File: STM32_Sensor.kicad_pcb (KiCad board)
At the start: 2 copper layers, 35.6 x 20.3 mm, 27 parts, among them J1 Conn Side, J2 Conn Down, J3 Conn Up, J4 Conn Prog, J5 u.FL, SW1 SW_Reset, SW2 SW_BOOT, U1 STM32F103C8Tx, U2 RFM69CW, U3 RFM69HW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

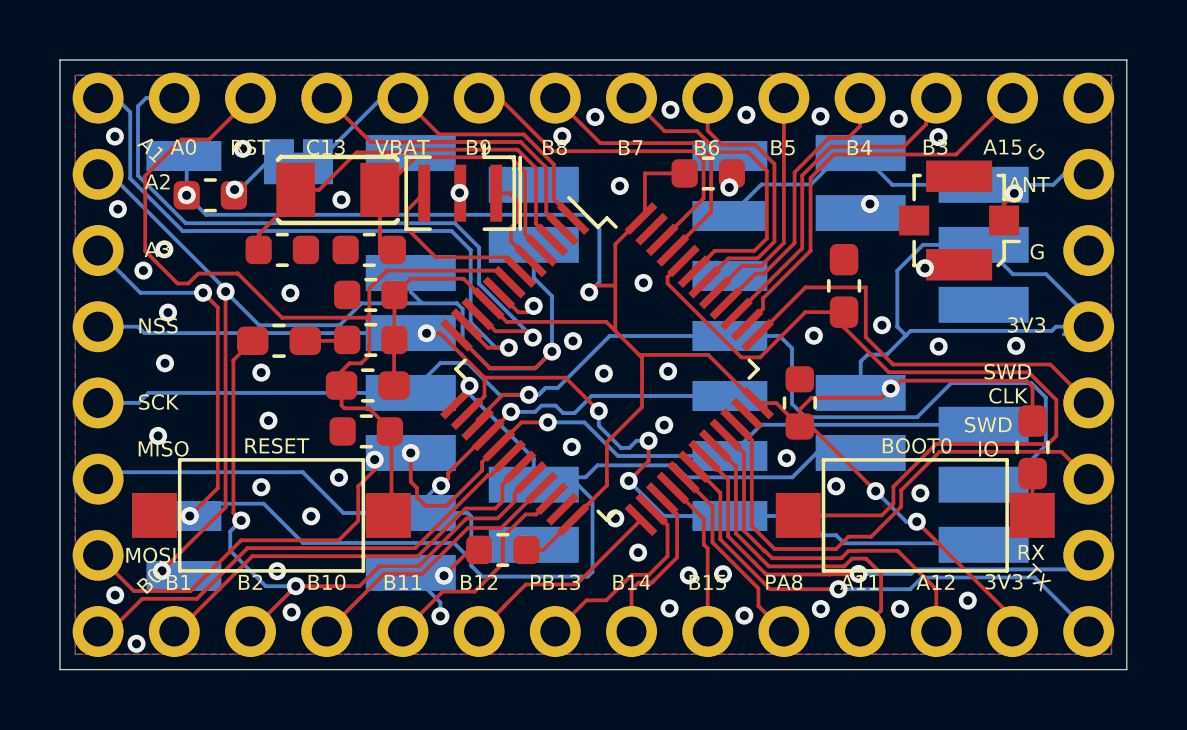
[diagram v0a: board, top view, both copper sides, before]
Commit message: Cleaned up project
Removed files that can be generated except for top and bottom
images which are referenced in the README.md
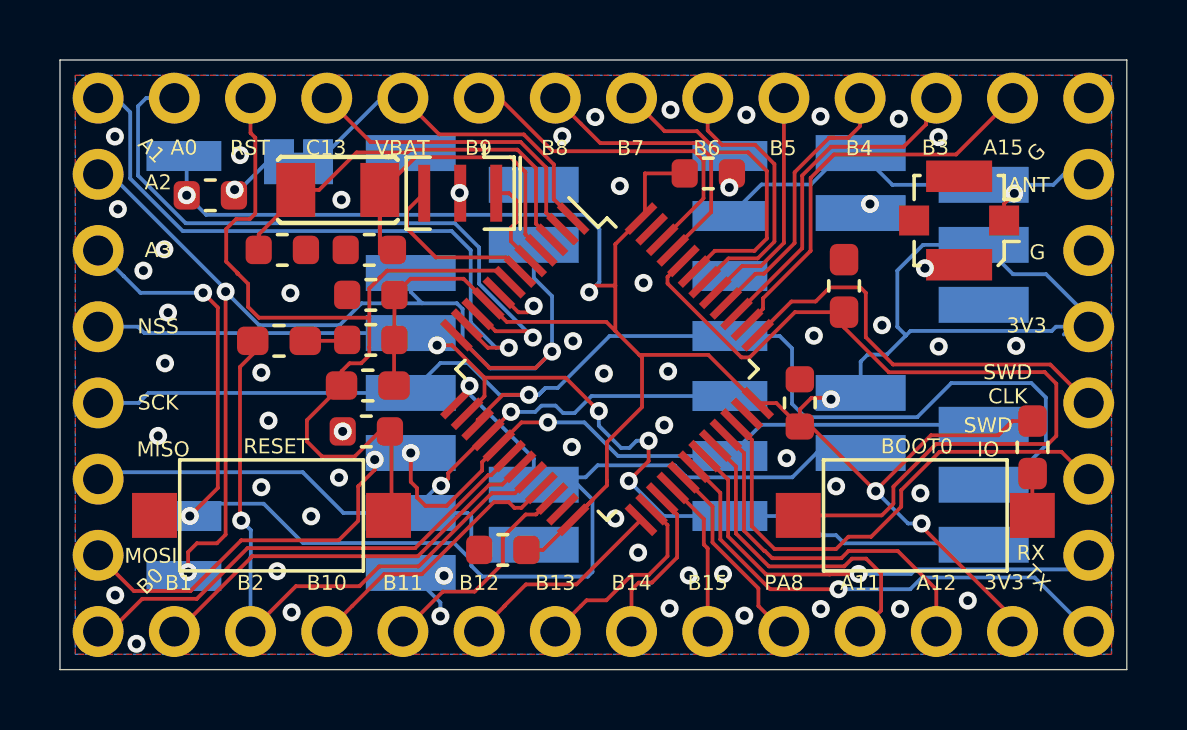
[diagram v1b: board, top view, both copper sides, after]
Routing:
- net +3V3: track 96.7 -> 94.8 mm
- net GND: track 7.47 -> 6.30 mm, vias 56 -> 57
- net RST: track 30.5 -> 29.9 mm
- net PB2: track 21.8 -> 21.5 mm, vias 2 -> 1
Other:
- board text added: "STM32 Sensor Node V5.0 by freynder"
- board text removed: "PB13"
- board text removed: "STM32 Sensor Node V4.5 by freynder"

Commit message: Made VBAT jumper NO
to comply with PCB manufacturer design rules.
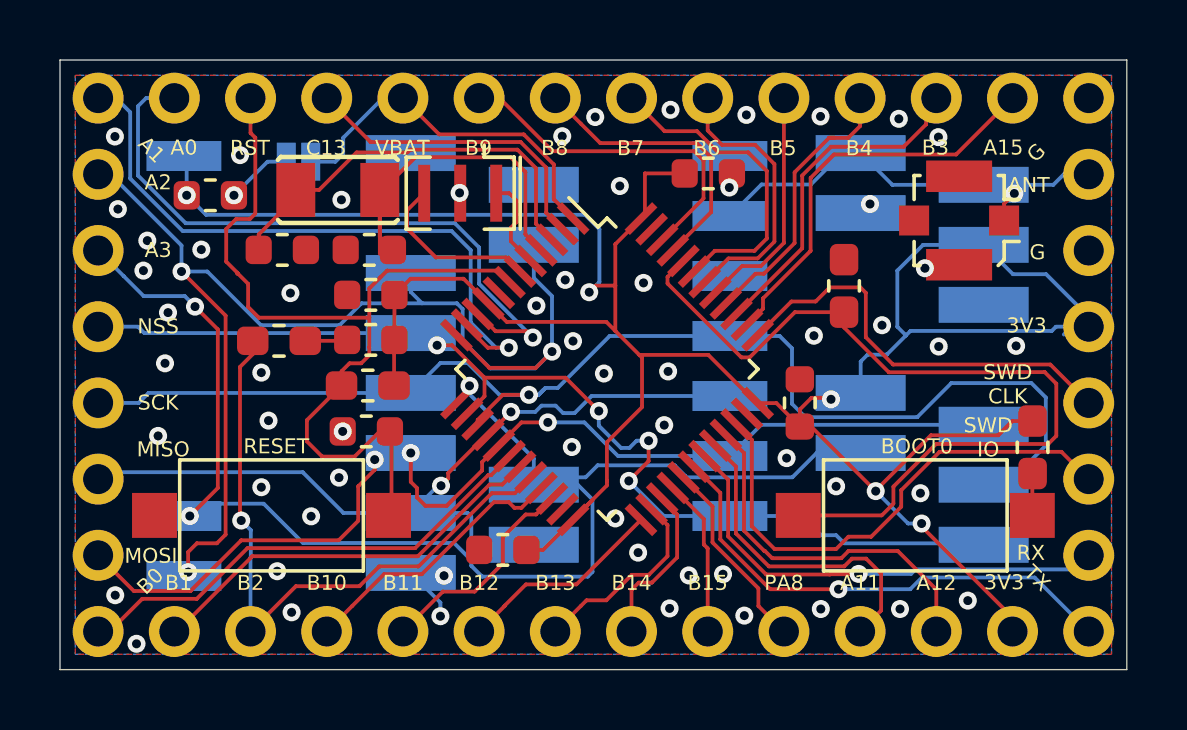
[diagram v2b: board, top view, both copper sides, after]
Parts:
- JP1: footprint Jumper:SolderJumper-2_P1.3mm_Bridged_Pad1.0x1.5mm -> Sparkfun Jumpers:SMT-JUMPER_2_NO_NO-SILK
- Y1: value 32768Mhz -> 32768 Crystal
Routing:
- net PA2: track 38.6 -> 40.4 mm
- net GND: track 6.30 -> 4.62 mm, vias 57 -> 59
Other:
- board text added: "STM32 Sensor Node V5.1 by freynder"
- board text removed: "STM32 Sensor Node V5.0 by freynder"
